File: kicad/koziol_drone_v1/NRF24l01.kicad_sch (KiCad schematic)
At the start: 1 part, among them U5 NRF24L01

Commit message: schemes progress
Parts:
- added C11: 10 nF, symbol Device:C
- added C12: 1 nF, symbol Device:C
- added C13, C14: 22 pF, symbol Device:C
- added C15: 2.2 nF, symbol Device:C
- added C16: 4.7 nF, symbol Device:C
- added C17, C22, C23, C24, C25: 1.5 pF, symbol Device:C
- added C18: 1 pF, symbol Device:C
- added C19: 220 pF, symbol Device:C
- added C20: 1 uF, symbol Device:C
- added C21: 0.3 pF, symbol Device:C
- added J1: Conn_Coaxial, Connector_Coaxial:SMA_Amphenol_901-143_Horizontal, symbol Connector:Conn_Coaxial
- added L1: 8.2 nH, symbol Device:L
- added L2: 2.7 Nh, symbol Device:L
- added L3: 3.9 nH, symbol Device:L
- added L4, L5: 2.4 nH, symbol Device:L
- added R2: 1M, symbol Device:R
- added R3: 22k, symbol Device:R
- added R4, R5: 1k, symbol Device:R
- added R6: 20K, symbol Device:R
- added U6: RFX2401C, RFX2401C:QFN50P300X300X60-17N, symbol RFX2401C:RFX2401C
- added Y1: Crystal, symbol Device:Crystal
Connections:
- net CE: now reaches U5.1 (CE)
- net CE: now also R5.1
- net at U5.10 (XC1): now also C14.1, R2.1, Y1.2
- net VDD_PA: now reaches U5.11 (VDD_PA)
- net VDD_PA: now also C15.1, C16.1, L2.2, R4.1
- net at U5.12 (ANT1): now also L1.1, L2.1
- net at U5.13 (ANT2): now also L1.2, L3.1
- net GND: now reaches U5.14 (VSS)
- net GND: now also U5.17 (VSS), U5.20 (VSS), U5.8 (VSS), C11.2, C12.2, C13.2, C14.2, C15.2, C16.2, C18.1, C19.2, C20.2, C21.2, C22.2, C23.2, C24.2, C25.2, J1.2 (Ext), R3.2, R6.2, U6.11 (GND), U6.17 (GND), U6.2 (GND), U6.3 (GND), U6.8 (GND), U6.9 (GND)
- net +3.3V: now reaches U5.15 (VDD)
- net +3.3V: now also U5.18 (VDD), U5.19 (DVDD), U5.7 (VDD), C11.1, C12.1, C19.1, C20.1, U6.14 (VDD), U6.16 (VDD)
- net at U5.16 (IREF): now also R3.1
- net CSN: now reaches U5.2 (CSN)
- net SCK: now reaches U5.3 (SCK)
- net MOSI: now reaches U5.4 (MOSI)
- net MISO: now reaches U5.5 (MISO)
- net IRQ: now reaches U5.6 (IRQ)
- net at U5.9 (XC2): now also C13.1, R2.2, Y1.1
- new net: C25.1, J1.1 (In), L5.2
- new net: C22.1, C23.1, C24.1, L4.2, L5.1
- new net: C17.1, L3.2
- new net: R5.2, R6.1, U6.6 (RXEN)
- new net: R4.2, U6.5 (TXEN)
- new net: C21.1, L4.1, U6.10 (ANT)
- new net RF_IO: C17.2, C18.2, U6.4 (TXRX)
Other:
- note added: "C13 I C14 MUSZA MATCHOWAC LOAD CAPACITANCE KRYSZTAŁU"
- moved on the sheet: U5

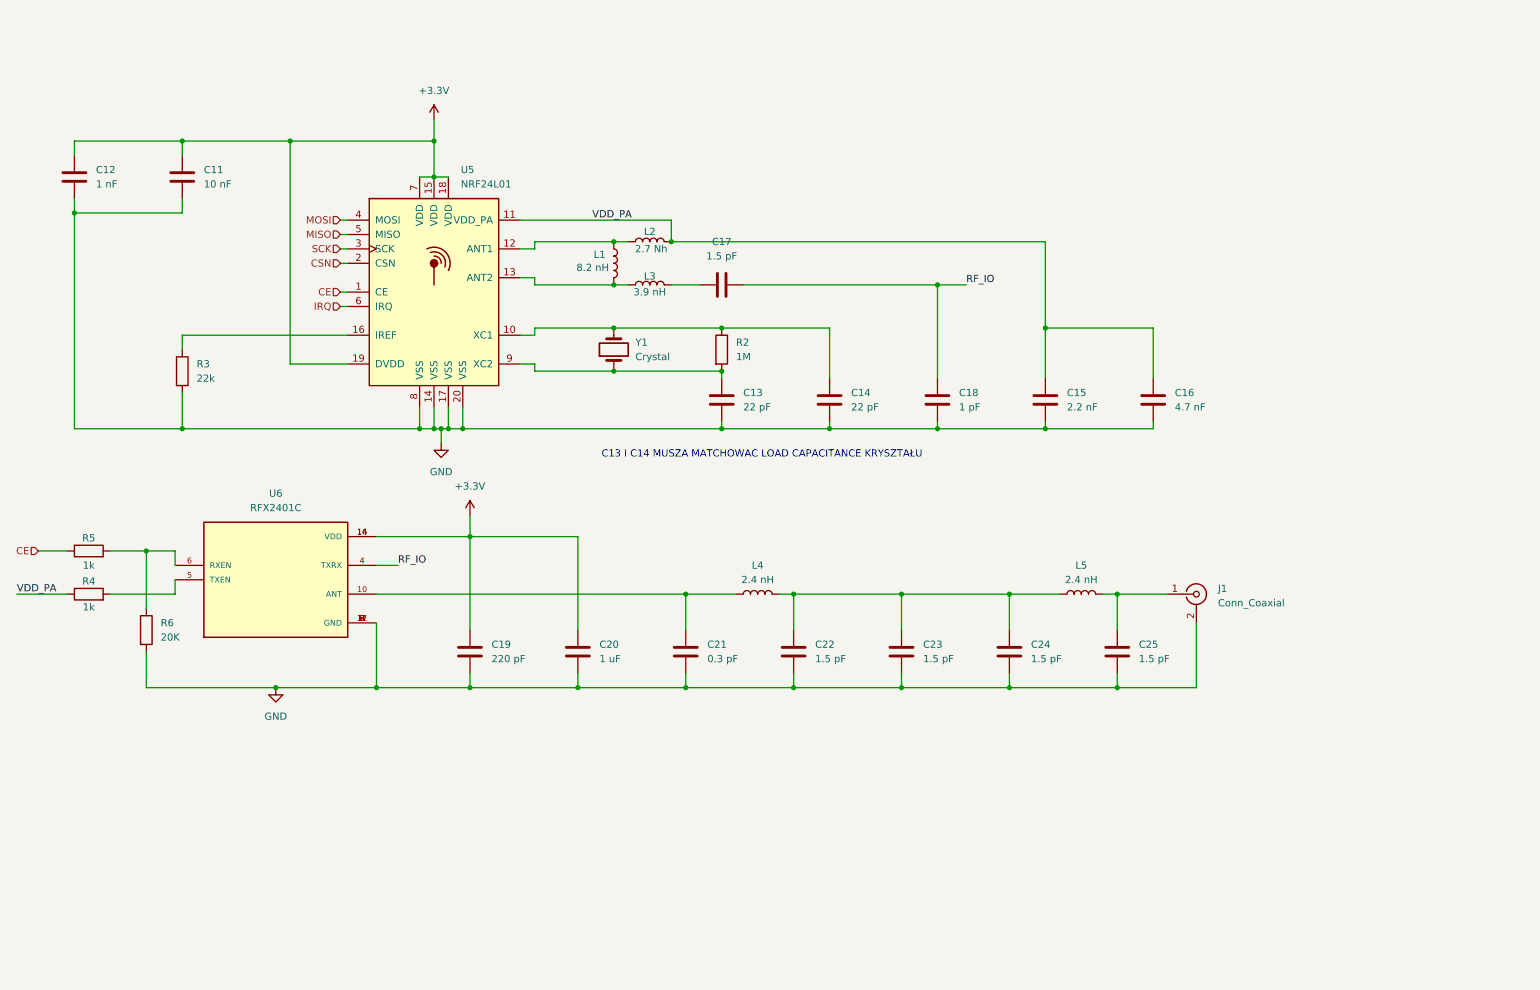
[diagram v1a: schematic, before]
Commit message: mcu scheme + buses
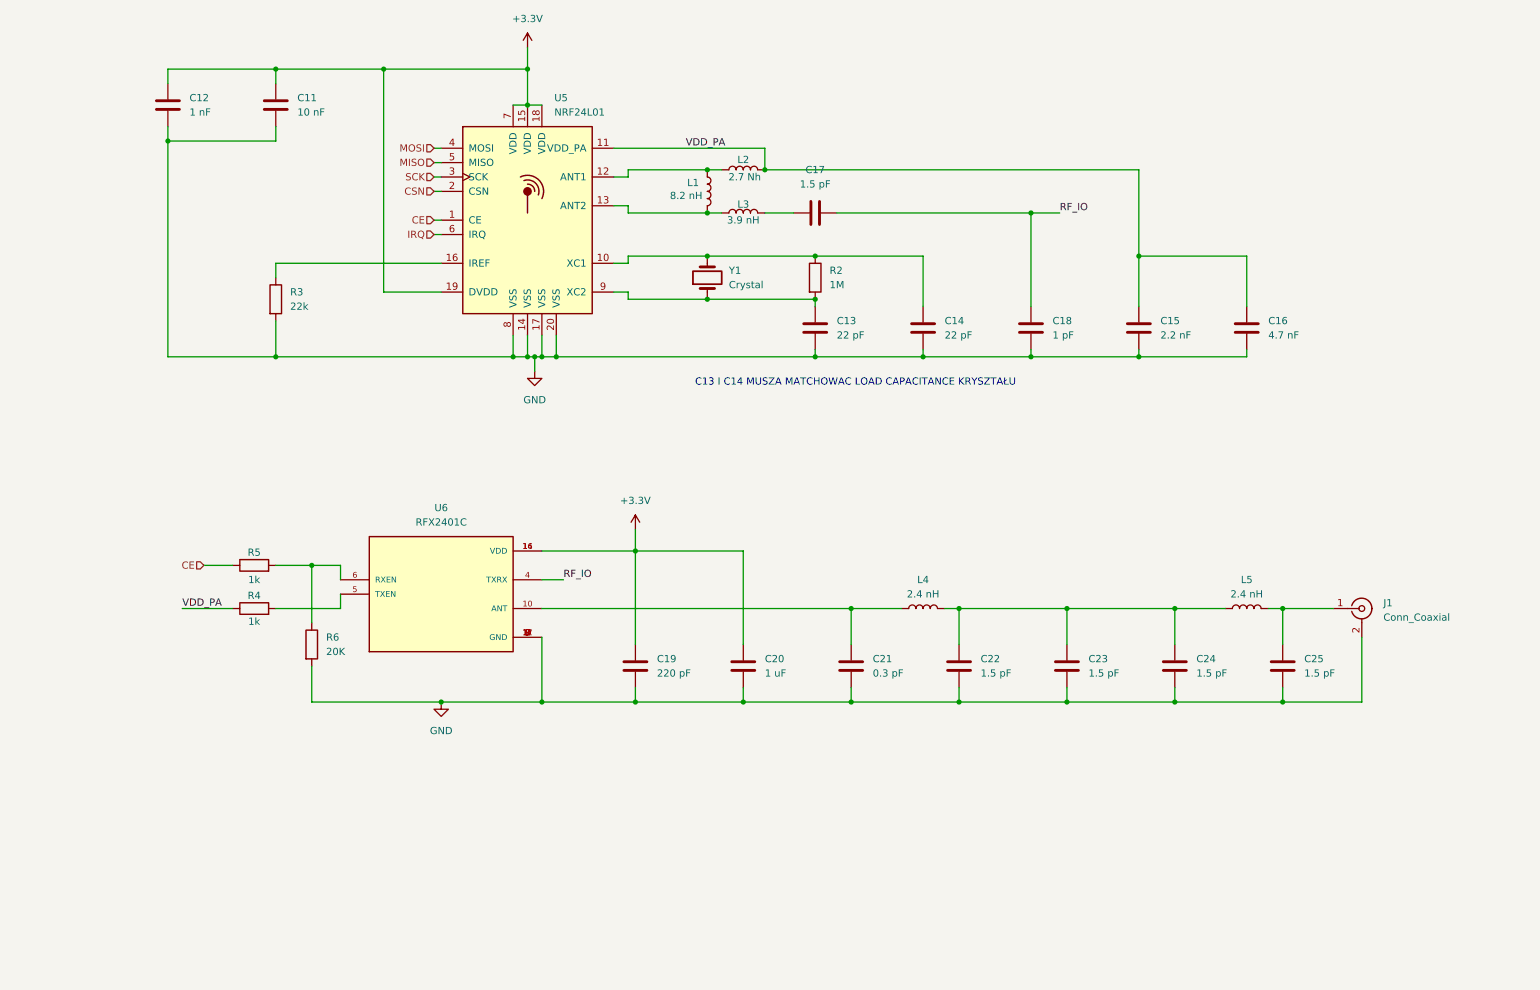
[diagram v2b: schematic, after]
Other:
- moved on the sheet: C11, C12, C13, C14, C15, C16, C17, C18, C19, C20, C21, C22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

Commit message: scheme descriptions and PDF plot
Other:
- note added: "NRF24I01"
- note added: "RF comunnication with high range addition."
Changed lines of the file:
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@@
+		)
+	)
+	(text "NRF24I01"
+		(exclude_from_sim no)
+		(at 186.182 189.992 0)
+		(effects
+			(font
+				(size 2.54 2.54)
+			)
+			(justify left)
+		)
+	)
+	(text "RF comunnication with high range addition."
+		(exclude_from_sim no)
+		(at 177.8 170.18 0)
+		(effects
+			(font
+				(size 2.54 2.54)
+			)
+			(justify left)
 		)
 	)
